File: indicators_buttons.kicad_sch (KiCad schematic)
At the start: 43 parts, among them SW1 BTN_PROGRAM, SW2 BTN_RESET, SW3 BTN_USER

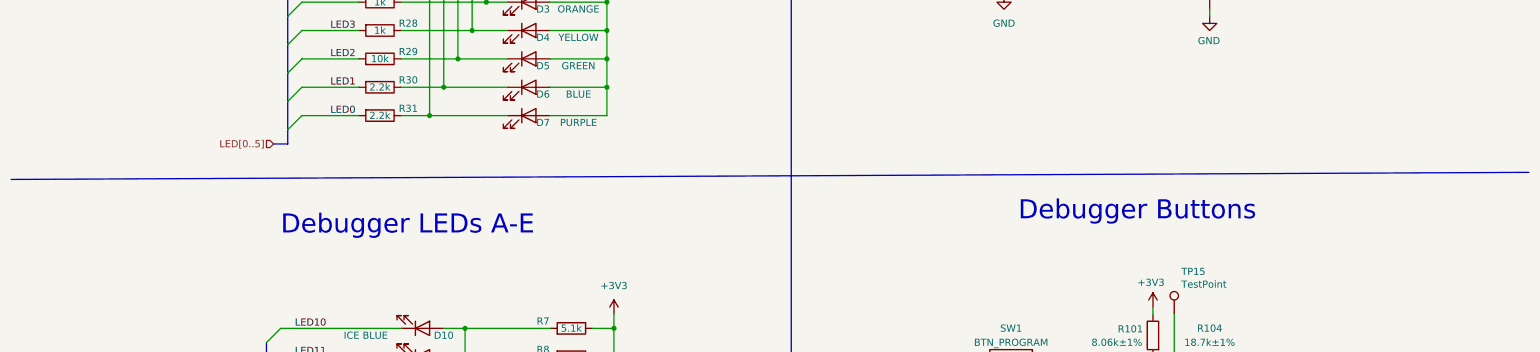
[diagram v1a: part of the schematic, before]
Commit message: Clean up schematic
- Renumber Pmod signal names to match silkscreen labels
- Clean up FPGA symbol
- Clean up PHY symbol
- Add title block to newer sheets
- Fix horizontal line in LED sheet
- Improve various label positions
- Update data sheet fields
- Renumber pages
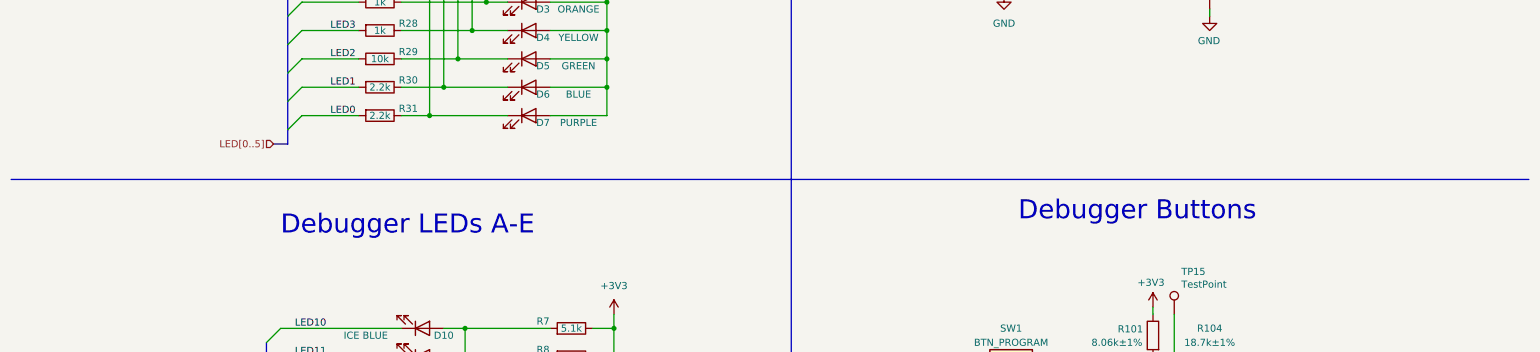
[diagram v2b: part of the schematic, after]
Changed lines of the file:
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@@
     (stroke (width 0) (type default))
   )
-  (polyline (pts (xy 12.7 96.52) (xy 284.48 95.25))
+  (polyline (pts (xy 12.7 96.52) (xy 284.48 96.52))
     (stroke (width 0) (type default))
   )

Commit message: Update copyright notices
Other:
- company: Copyright 2019-2023 Great Scott Gadgets -> ${COPYRIGHT}
- title: Cynthion -> ${TITLE}
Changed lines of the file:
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@@
   (paper "A4")
   (title_block
-    (title "Cynthion")
+    (title "${TITLE}")
     (date "${DATE}")
     (rev "${VERSION}")
-    (company "Copyright 2019-2023 Great Scott Gadgets")
-    (comment 1 "Licensed under the CERN-OHL-P v2")
+    (company "${COPYRIGHT}")
+    (comment 1 "${LICENSE}")
   )
   (junction (at 220.98 129.54) (diameter 0) (color 0 0 0 0)
